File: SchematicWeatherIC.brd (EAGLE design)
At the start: 47.9 x 64.8 mm, 32 parts

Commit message: this is where the routing updates are in progress
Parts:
- moved R8 15.3 mm to (38.1, 21.6), turned to 270 degrees
- moved C14 10.5 mm to (2.54, 17.8)
- moved LDO 10.5 mm to (15.2, 5.08)
- moved R7 8.98 mm to (27.9, 24.1)
- moved BME280 8.52 mm to (30.5, 29.2)
- moved R9 7.62 mm to (27.9, 19.1)
- moved BUTTON 5.24 mm to (22.9, 5.08)
- moved USBTOSERIAL 3.81 mm to (8.89, 17.8)
- moved ESP32 2.54 mm to (17.8, 20.3)
- moved R6 1.80 mm to (35.6, 31.8), turned to 90 degrees
- moved C10 1.27 mm to (35.6, 47.0)
- moved R3 1.27 mm to (34.3, 12.7)
- moved R4 1.27 mm to (34.3, 7.62)
- moved R5 1.27 mm to (34.3, 2.54)
- moved C12 1.27 mm to (35.6, 40.6)
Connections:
- new net N$20: ESP32.17, USBTOSERIAL.4
- new net N$21: ESP32.16, USBTOSERIAL.5
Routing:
- net GND: track 187.3 -> 2.22 mm, vias 1 -> 0
- net VDD: track 173.0 -> 0.45 mm
- net N$2: track 123.9 -> 1.39 mm
- net N$10: track 83.5 -> 0.00 mm
- net SCL: track 76.9 -> 0.88 mm, vias 1 -> 0
- net N$17: track 74.9 -> 0.10 mm, vias 1 -> 0
- net N$9: track 67.1 -> 0.00 mm
- net N$8: track 66.2 -> 0.00 mm
- net N$12: track 63.5 -> 0.34 mm, vias 1 -> 0
- net SDA: track 61.6 -> 0.86 mm, vias 1 -> 0
- net N$13: track 47.5 -> 0.53 mm
- net N$6: track 45.6 -> 0.00 mm
- net N$15: track 43.1 -> 0.10 mm, vias 2 -> 0
- net N$11: track 42.0 -> 0.10 mm, vias 1 -> 0
- net N$14: track 35.8 -> 0.10 mm
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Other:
- board size 47.9 x 64.8 mm -> 45.4 x 64.8 mm

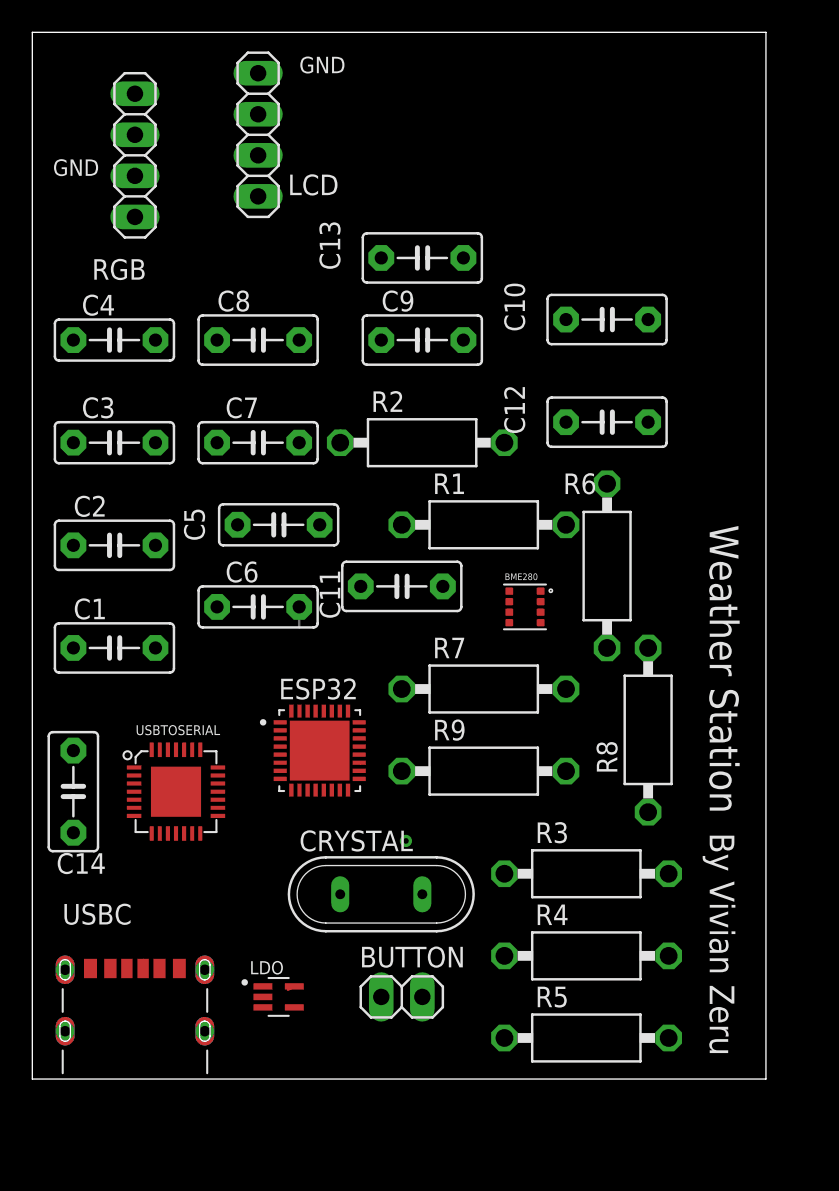
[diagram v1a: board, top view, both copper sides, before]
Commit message: routed differential pair and i2c
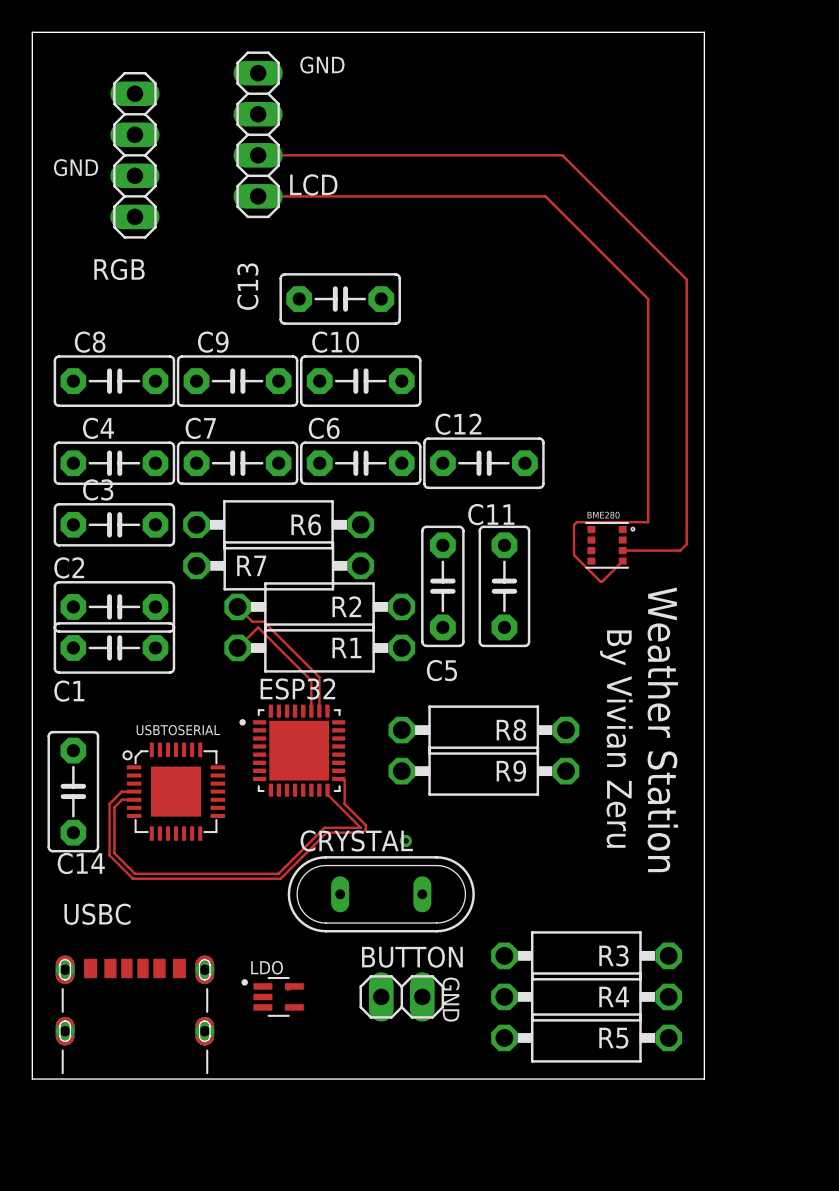
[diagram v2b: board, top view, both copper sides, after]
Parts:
- moved R6 20.5 mm to (15.2, 34.3), turned to 0 degrees
- moved C10 15.7 mm to (20.3, 43.2)
- moved R7 14.8 mm to (15.2, 31.8), turned to 180 degrees
- moved R1 12.7 mm to (17.8, 26.7)
- moved R2 12.0 mm to (17.8, 29.2)
- moved C9 11.7 mm to (12.7, 43.2)
- moved C6 10.9 mm to (20.3, 38.1)
- moved C5 10.9 mm to (25.4, 30.5), turned to 90 degrees
- moved R8 10.2 mm to (27.9, 21.6), turned to 0 degrees
- moved C8 9.25 mm to (5.08, 43.2)
- moved C12 8.03 mm to (27.9, 38.1)
- moved C4 7.62 mm to (5.08, 38.1)
- moved BME280 6.35 mm to (35.6, 33.0)
- moved C11 6.35 mm to (29.2, 30.5), turned to 90 degrees
- moved C13 5.68 mm to (19.1, 48.3)
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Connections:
- net N$20 renamed D_P
- net N$21 renamed D_N
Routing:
- net SCL: track 0.88 -> 59.8 mm
- net SDA: track 0.86 -> 59.3 mm
- net D_P: track 0.00 -> 26.7 mm
- net D_N: track 0.00 -> 24.4 mm
- net GND: track 2.22 -> 0.95 mm
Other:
- board size 45.4 x 64.8 mm -> 41.6 x 64.8 mm

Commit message: Add files via upload
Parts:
- moved BME280 1.27 mm to (36.8, 33.0)
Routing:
- net SDA: track 59.3 -> 58.0 mm
- net N$2: track 1.39 -> 0.59 mm
